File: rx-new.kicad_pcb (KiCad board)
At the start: 2 copper layers, 76.2 x 50.8 mm, 96 parts, among them J1 RF_IN, J2 PWR_IN, J3 IQ_OUT, J4 4LO_IN, Q1 BC848, Q2 BC858, Q3 BC848, Q4 BC858, U1 TPS79101DBVREP, U2 SN74CBT3253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

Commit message: WIP on layout
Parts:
- moved R17 90.3 mm to (184.2, 36.8)
- moved J3 87.6 mm to (153.0, 24.1), turned to 90 degrees
- moved C45 81.3 mm to (196.1, 59.0)
- moved C9 81.3 mm to (171.8, 78.0)
- moved J2 81.3 mm to (163.8, 59.2)
- moved Q1 81.3 mm to (204.3, 85.7)
- moved C11 81.3 mm to (168.0, 93.7)
- moved C12 81.3 mm to (184.6, 68.4)
- moved C13 81.3 mm to (210.9, 58.3)
- moved C15 81.3 mm to (206.2, 58.3)
- moved C16 81.3 mm to (194.7, 69.1)
- moved C17 81.3 mm to (183.3, 90.5)
- moved C18 81.3 mm to (184.6, 72.6)
- moved C19 81.3 mm to (177.7, 78.0)
- moved C41 81.3 mm to (194.7, 72.1)
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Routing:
- net /-Vf: track 0.00 -> 33.8 mm
- net /+Vd: track 0.00 -> 33.6 mm
- net GND: track 0.00 -> 27.0 mm, vias 0 -> 2
- net Net-(TR1-Pad4): track 0.00 -> 24.0 mm
- net Net-(TR1-Pad6): track 0.00 -> 23.9 mm
- net Net-(C30-Pad1): track 0.00 -> 19.4 mm
- net Net-(C29-Pad2): track 0.00 -> 18.6 mm
- net Net-(U7-Pad2): track 0.00 -> 15.5 mm
- net /+Vf: track 0.00 -> 14.5 mm
- net /270deg: track 0.00 -> 12.7 mm
- net Net-(C2-Pad1): track 0.00 -> 11.6 mm
- net /180deg: track 0.00 -> 11.2 mm
- net Net-(U7-Pad3): track 0.00 -> 11.1 mm
- net Net-(C2-Pad2): track 0.00 -> 10.6 mm
- net /AUDIO_Q: track 0.00 -> 9.71 mm
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- added copper zone on B.Cu, net GND

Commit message: some_layouting
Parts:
- moved R20 122.0 mm to (73.0, 87.6), turned to 270 degrees
- moved R13 117.5 mm to (97.8, 69.2)
- moved C17 106.9 mm to (77.5, 75.6), turned to 180 degrees
- moved R18 104.9 mm to (104.1, 67.3)
- moved R10 101.4 mm to (99.1, 88.9)
- moved R19 97.7 mm to (116.2, 62.9), turned to 180 degrees
- moved R11 95.1 mm to (104.8, 85.7)
- moved R14 92.8 mm to (104.1, 77.5)
- moved R16 90.0 mm to (104.1, 74.9)
- moved R22 86.4 mm to (111.8, 62.9), turned to 180 degrees
- moved R17 84.7 mm to (109.9, 77.5)
- moved R21 82.1 mm to (109.9, 74.9), turned to 180 degrees
- moved R15 81.0 mm to (116.2, 60.3)
- moved J3 63.1 mm to (95.9, 50.8)
- moved R23 60.7 mm to (106.7, 70.9)
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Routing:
- net /-Vf: track 33.8 -> 70.8 mm
- net Net-(R18-Pad2): track 0.00 -> 19.2 mm
- net /0deg: track 6.93 -> 25.9 mm
- net /Vbias: track 0.00 -> 13.8 mm
- net Net-(C29-Pad2): track 18.6 -> 4.97 mm
- net Net-(R20-Pad2): track 3.99 -> 17.3 mm
- net /180deg: track 11.2 -> 23.9 mm
- net /270deg: track 12.7 -> 25.2 mm
- net Net-(R16-Pad2): track 0.00 -> 12.3 mm
- net /CLK_0: track 3.31 -> 13.2 mm, vias 2 -> 0
- net /AUDIO_Q: track 9.71 -> 0.00 mm
- net Net-(R12-Pad2): track 6.57 -> 14.8 mm
- net Net-(R13-Pad2): track 0.00 -> 8.07 mm
- net /CLK_1: track 4.53 -> 12.4 mm, vias 2 -> 0
- net /AUDIO_I: track 6.60 -> 0.00 mm
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- removed copper zone on B.Cu, net GND

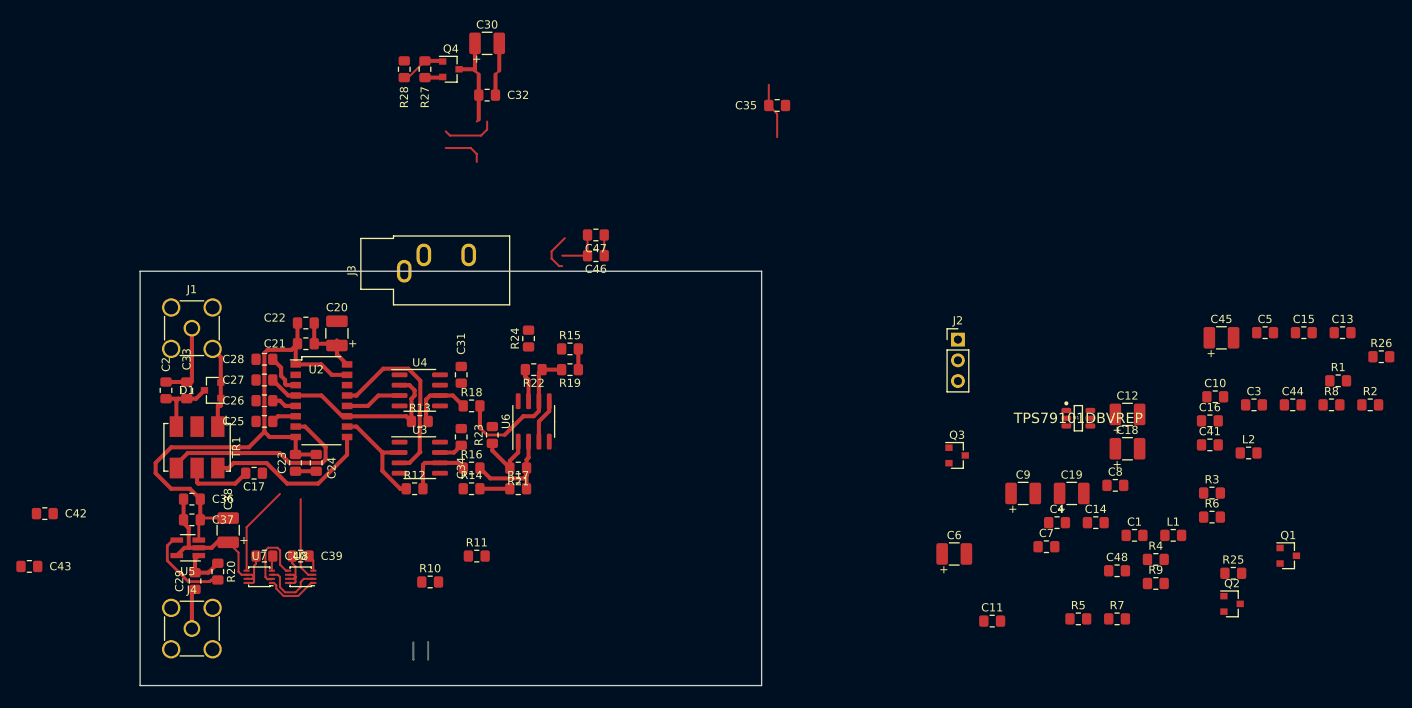
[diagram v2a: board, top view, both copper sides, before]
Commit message: Layout: worked on power section
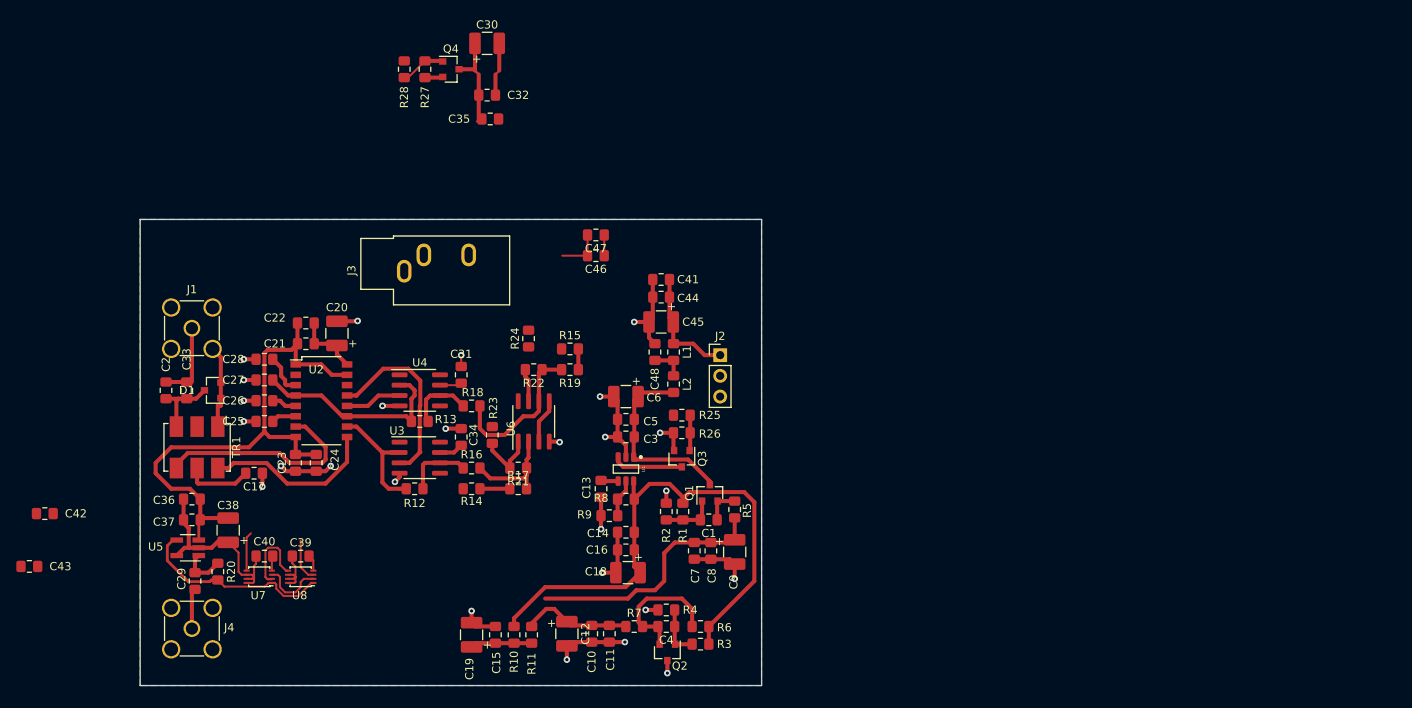
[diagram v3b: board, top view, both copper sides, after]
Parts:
- moved C15 105.8 mm to (107.1, 95.4), turned to 270 degrees
- moved C13 92.9 mm to (120.0, 77.5), turned to 90 degrees
- moved R2 87.3 mm to (128.0, 80.3), turned to 90 degrees
- moved R8 87.3 mm to (123.1, 78.7), turned to 180 degrees
- moved R26 86.3 mm to (129.9, 70.6), turned to 180 degrees
- moved R1 81.9 mm to (130.0, 80.3), turned to 270 degrees
- moved C10 81.8 mm to (118.9, 95.2), turned to 90 degrees
- moved C5 79.1 mm to (123.1, 69.0)
- moved C44 78.6 mm to (127.4, 54.0)
- moved C3 77.1 mm to (123.1, 71.1)
- moved C19 75.6 mm to (104.1, 95.4), turned to 90 degrees
- moved C12 73.8 mm to (115.8, 95.2), turned to 270 degrees
- moved C16 73.3 mm to (123.1, 85.0)
- moved Q1 71.3 mm to (133.3, 78.0), turned to 90 degrees
- moved L2 71.0 mm to (128.9, 64.6), turned to 270 degrees
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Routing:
- net GND: track 21.9 -> 105.5 mm, vias 0 -> 26
- net /+Vf: track 14.5 -> 82.0 mm
- net /+Vd: track 30.0 -> 61.0 mm
- net /Vbat: track 2.21 -> 25.4 mm
- net Net-(C4-Pad2): track 0.00 -> 16.4 mm
- net Net-(C41-Pad2): track 0.00 -> 14.4 mm
- net /-Vf: track 70.8 -> 84.4 mm
- net /Eo: track 0.00 -> 8.66 mm
- net /CLK_0: track 13.2 -> 4.81 mm
- net /Vbias: track 13.8 -> 21.3 mm
- net /CLK_1: track 12.4 -> 5.20 mm
- net Net-(R20-Pad2): track 17.3 -> 24.5 mm
- net Net-(R12-Pad2): track 14.8 -> 8.23 mm
- net Net-(C1-Pad2): track 0.00 -> 6.57 mm
- net Net-(C4-Pad1): track 0.00 -> 6.32 mm
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- added copper zone on B.Cu, net GND
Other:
- board size 76.2 x 50.8 mm -> 76.2 x 57.1 mm

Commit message: Layout: more work
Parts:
- moved J3 44.1 mm to (94.6, 94.9), turned to 180 degrees
- moved C35 39.9 mm to (104.1, 72.0)
- moved C30 39.8 mm to (108.0, 62.6), turned to 90 degrees
- moved R28 37.1 mm to (118.2, 55.6), turned to 90 degrees
- moved C32 34.3 mm to (105.0, 63.5), turned to 270 degrees
- moved R27 34.3 mm to (115.7, 55.6), turned to 90 degrees
- moved Q4 31.5 mm to (112.5, 55.6), turned to 180 degrees
- moved C47 25.1 mm to (108.6, 69.0), turned to 0 degrees
- moved C46 20.7 mm to (108.6, 66.5), turned to 0 degrees
- moved R24 19.3 mm to (106.6, 77.9), turned to 270 degrees
- moved R14 8.69 mm to (111.9, 81.4), turned to 180 degrees
- moved R23 7.27 mm to (108.7, 77.9), turned to 270 degrees
- moved C6 2.74 mm to (125.7, 65.5), turned to 90 degrees
- moved R17 2.62 mm to (111.9, 79.1)
- moved R21 2.62 mm to (111.9, 76.6)
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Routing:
- net /+Vf: track 82.0 -> 163.6 mm
- net /Vbias: track 21.3 -> 61.0 mm
- net /AUDIO_I: track 0.00 -> 21.8 mm
- net /Eo: track 8.66 -> 29.4 mm
- net /AUDIO_Q: track 0.00 -> 20.4 mm
- net /Vbat: track 25.4 -> 45.7 mm
- net /-Vf: track 84.4 -> 99.0 mm, vias 0 -> 2
- net Net-(C30-Pad1): track 18.2 -> 30.1 mm
- net /En: track 0.00 -> 6.67 mm
- net Net-(U7-Pad2): track 9.29 -> 2.77 mm
- net Net-(U7-Pad3): track 7.77 -> 2.34 mm
- net Net-(R16-Pad2): track 12.3 -> 16.9 mm
- net /+Vd: track 61.0 -> 65.2 mm
- net Net-(R18-Pad2): track 19.2 -> 23.0 mm
- net /CLK_1: track 5.20 -> 1.93 mm
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
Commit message: finished_layout
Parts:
- C42: value 0.1u -> 1n
- moved C43 56.6 mm to (95.9, 54.0)
- moved C12 53.2 mm to (78.7, 57.1), turned to 180 degrees
- moved R3 52.9 mm to (106.7, 50.2), turned to 90 degrees
- moved R6 47.8 mm to (107.3, 53.6), turned to 0 degrees
- moved Q2 47.5 mm to (114.0, 52.2), turned to 0 degrees
- moved R11 46.7 mm to (70.5, 73.0)
- moved R4 45.5 mm to (114.3, 48.9), turned to 0 degrees
- moved C4 45.4 mm to (110.9, 52.3), turned to 270 degrees
- moved C10 44.9 mm to (94.1, 57.8)
- moved C11 44.9 mm to (96.3, 57.8)
- moved U7 43.3 mm to (101.0, 51.4), turned to 0 degrees
- moved R7 43.3 mm to (104.1, 55.9)
- moved J4 41.3 mm to (69.8, 53.3), turned to 270 degrees
- moved R20 40.1 mm to (80.6, 48.3), turned to 0 degrees
- moved U8 39.0 mm to (95.9, 51.4), turned to 0 degrees
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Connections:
- C42 pad 1: /-Vf -> GND
- C42 pad 2: /+Vd -> /-Vf
- U2 pad 7: Net-(TR1-Pad4) -> Net-(TR1-Pad6)
- U2 pad 9: Net-(TR1-Pad6) -> Net-(TR1-Pad4)
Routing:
- net /+Vd: track 65.2 -> 134.0 mm, vias 0 -> 2
- net /+Vf: track 163.6 -> 122.7 mm
- net /CLK_1: track 1.93 -> 29.7 mm, vias 0 -> 2
- net /Vbias: track 61.0 -> 85.0 mm
- net /CLK_0: track 4.05 -> 25.4 mm, vias 0 -> 2
- net /En: track 6.67 -> 17.9 mm
- net /180deg: track 19.9 -> 31.0 mm, vias 0 -> 2
- net /-Vf: track 99.0 -> 89.5 mm
- net Net-(TR1-Pad6): track 21.3 -> 30.1 mm
- net /90deg: track 10.0 -> 18.4 mm, vias 0 -> 2
- net Net-(U7-Pad3): track 2.34 -> 10.5 mm, vias 0 -> 2
- net /0deg: track 25.9 -> 33.8 mm, vias 0 -> 2
- net /AUDIO_Q: track 20.4 -> 28.1 mm
- net Net-(TR1-Pad4): track 26.2 -> 19.0 mm
- net /Eo: track 29.4 -> 23.9 mm
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
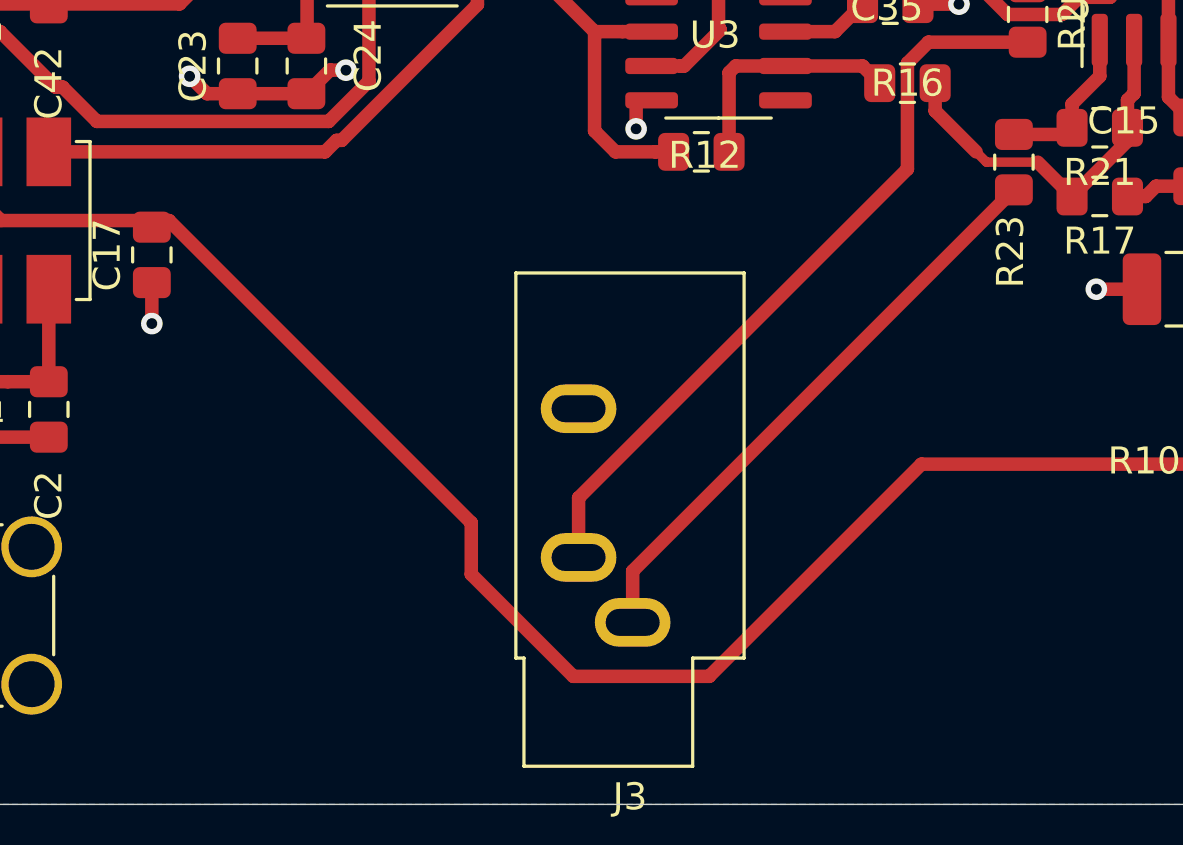
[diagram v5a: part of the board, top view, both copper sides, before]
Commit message: Fixed audio jack pin assignment
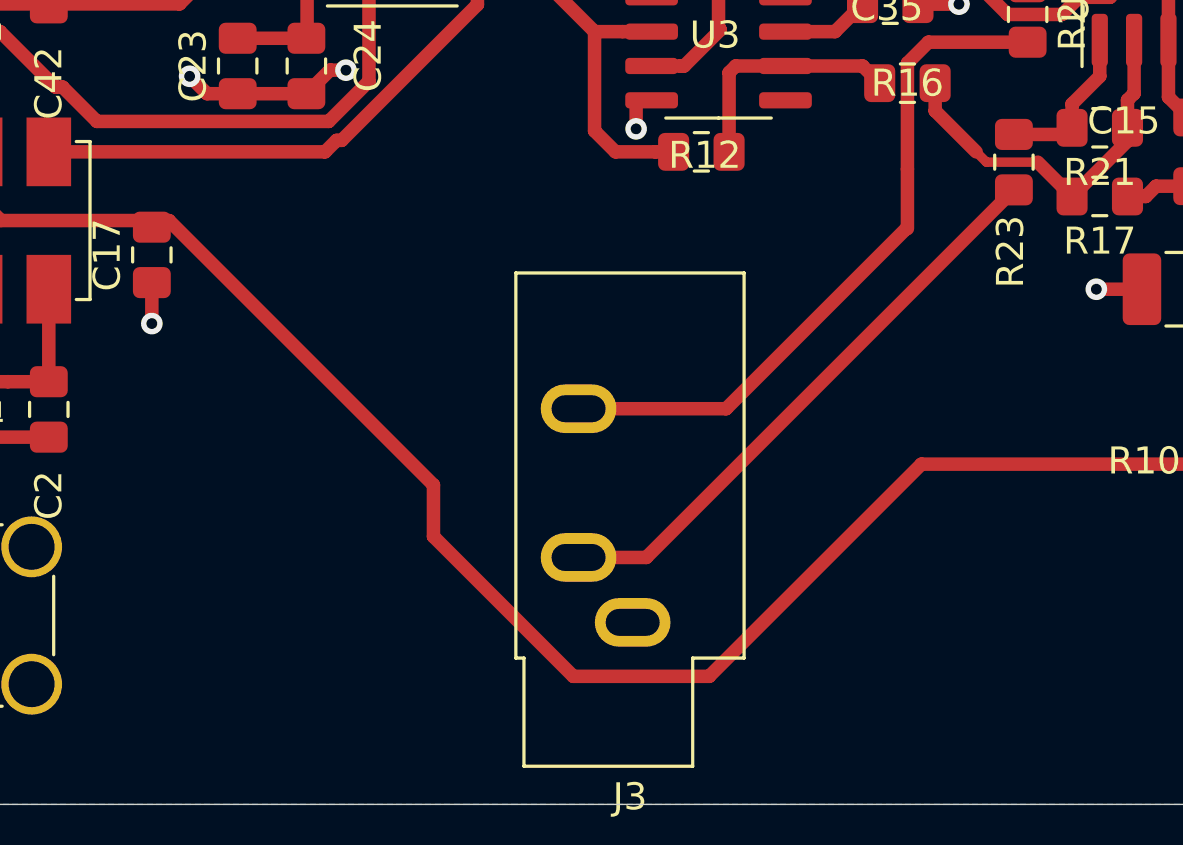
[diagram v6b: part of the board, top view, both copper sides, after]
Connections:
- J3 pad R: GND -> /AUDIO_Q
- J3 pad S: /AUDIO_I -> GND
- J3 pad T: /AUDIO_Q -> /AUDIO_I
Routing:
- net /AUDIO_Q: track 28.1 -> 25.8 mm
